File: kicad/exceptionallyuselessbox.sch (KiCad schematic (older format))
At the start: 10 parts, among them J1 Conn_01x02, J2 Conn_01x04, J3 Conn_01x02, J4 Conn_01x03, J5 Conn_01x03, U1 DSN-MINI-360

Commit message: Complete PCB.
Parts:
- C1, C2: value CP -> 100u; footprint (none) -> Capacitor_THT:CP_Radial_D8.0mm_P5.00mm
- J1, J3: footprint (none) -> Connector_JST:JST_XH_B02B-XH-A_1x02_P2.50mm_Vertical
- J2: footprint (none) -> Connector_JST:JST_XH_B04B-XH-A_1x04_P2.50mm_Vertical
- J4, J5: footprint (none) -> Connector_JST:JST_XH_B03B-XH-A_1x03_P2.50mm_Vertical
- R1: footprint (none) -> Resistor_THT:R_Axial_DIN0309_L9.0mm_D3.2mm_P12.70mm_Horizontal
- U1: footprint (none) -> Module:DSN-MINI-360
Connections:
- net +5V: no longer C2.1
- net +6V: now also C2.1
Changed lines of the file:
@@
 F 0 "J1" H 2568 2867 50  0000 C CNN
 F 1 "Conn_01x02" H 2568 2776 50  0000 C CNN
-F 2 "" H 2650 2650 50  0001 C CNN
+F 2 "Connector_JST:JST_XH_B02B-XH-A_1x02_P2.50mm_Vertical" H 2650 2650 50  0001 C CNN
 F 3 "~" H 2650 2650 50  0001 C CNN
 	1    2650 2650
@@
 F 0 "J2" H 2568 3817 50  0000 C CNN
 F 1 "Conn_01x04" H 2568 3726 50  0000 C CNN
-F 2 "" H 2650 3500 50  0001 C CNN
+F 2 "Connector_JST:JST_XH_B04B-XH-A_1x04_P2.50mm_Vertical" H 2650 3500 50  0001 C CNN
 F 3 "~" H 2650 3500 50  0001 C CNN
 	1    2650 3500
@@
 F 0 "R1" H 3420 2446 50  0000 L CNN
 F 1 "10k" H 3420 2355 50  0000 L CNN
-F 2 "" V 3280 2400 50  0001 C CNN
+F 2 "Resistor_THT:R_Axial_DIN0309_L9.0mm_D3.2mm_P12.70mm_Horizontal" V 3280 2400 50  0001 C CNN
 F 3 "~" H 3350 2400 50  0001 C CNN
 	1    3350 2400
@@
 F 0 "J4" H 5980 3042 50  0000 L CNN
 F 1 "Conn_01x03" H 5980 2951 50  0000 L CNN
-F 2 "" H 5900 3000 50  0001 C CNN
+F 2 "Connector_JST:JST_XH_B03B-XH-A_1x03_P2.50mm_Vertical" H 5900 3000 50  0001 C CNN
 F 3 "~" H 5900 3000 50  0001 C CNN
 	1    5900 3000
@@
 F 0 "J5" H 5980 3742 50  0000 L CNN
 F 1 "Conn_01x03" H 5980 3651 50  0000 L CNN
-F 2 "" H 5900 3700 50  0001 C CNN
+F 2 "Connector_JST:JST_XH_B03B-XH-A_1x03_P2.50mm_Vertical" H 5900 3700 50  0001 C CNN
 F 3 "~" H 5900 3700 50  0001 C CNN
 	1    5900 3700
@@
 P 7250 2400
 F 0 "C1" H 7368 2446 50  0000 L CNN
-F 1 "CP" H 7368 2355 50  0000 L CNN
-F 2 "" H 7288 2250 50  0001 C CNN
+F 1 "100u" H 7368 2355 50  0000 L CNN
+F 2 "Capacitor_THT:CP_Radial_D8.0mm_P5.00mm" H 7288 2250 50  0001 C CNN
 F 3 "~" H 7250 2400 50  0001 C CNN
 	1    7250 2400
@@
 P 7850 2400
 F 0 "C2" H 7968 2446 50  0000 L CNN
-F 1 "CP" H 7968 2355 50  0000 L CNN
-F 2 "" H 7888 2250 50  0001 C CNN
+F 1 "100u" H 7968 2355 50  0000 L CNN
+F 2 "Capacitor_THT:CP_Radial_D8.0mm_P5.00mm" H 7888 2250 50  0001 C CNN
 F 3 "~" H 7850 2400 50  0001 C CNN
 	1    7850 2400
@@
 	1    0    0    -1
 $EndComp
-$Comp
-L power:+5V #PWR016
-U 1 1 5D1A2DBA
-P 7850 2050
-F 0 "#PWR016" H 7850 1900 50  0001 C CNN
-F 1 "+5V" H 7865 2223 50  0000 C CNN
-F 2 "" H 7850 2050 50  0001 C CNN
-F 3 "" H 7850 2050 50  0001 C CNN
-	1    7850 2050
-	1    0    0    -1
-$EndComp
 Wire Wire Line
 	7850 2050 7850 2250
@@
 F 0 "J3" H 2568 5617 50  0000 C CNN
 F 1 "Conn_01x02" H 2568 5526 50  0000 C CNN
-F 2 "" H 2650 5400 50  0001 C CNN
+F 2 "Connector_JST:JST_XH_B02B-XH-A_1x02_P2.50mm_Vertical" H 2650 5400 50  0001 C CNN
 F 3 "~" H 2650 5400 50  0001 C CNN
 	1    2650 5400
@@
 F 0 "U1" H 3600 5765 50  0000 C CNN
 F 1 "DSN-MINI-360" H 3600 5674 50  0000 C CNN
-F 2 "" H 3600 5450 50  0001 C CNN
+F 2 "Module:DSN-MINI-360" H 3600 5450 50  0001 C CNN
 F 3 "regulator\\lm78xx.pdf" H 3600 5450 50  0001 C CNN
 	1    3600 5450
@@
 Wire Wire Line
 	5900 1900 5900 2000
+$Comp
+L power:+6V #PWR?
+U 1 1 5D20DD0B
+P 7850 2050
+F 0 "#PWR?" H 7850 1900 50  0001 C CNN
+F 1 "+6V" H 7865 2223 50  0000 C CNN
+F 2 "" H 7850 2050 50  0001 C CNN
+F 3 "" H 7850 2050 50  0001 C CNN
+	1    7850 2050
+	1    0    0    -1
+$EndComp
 $EndSCHEMATC

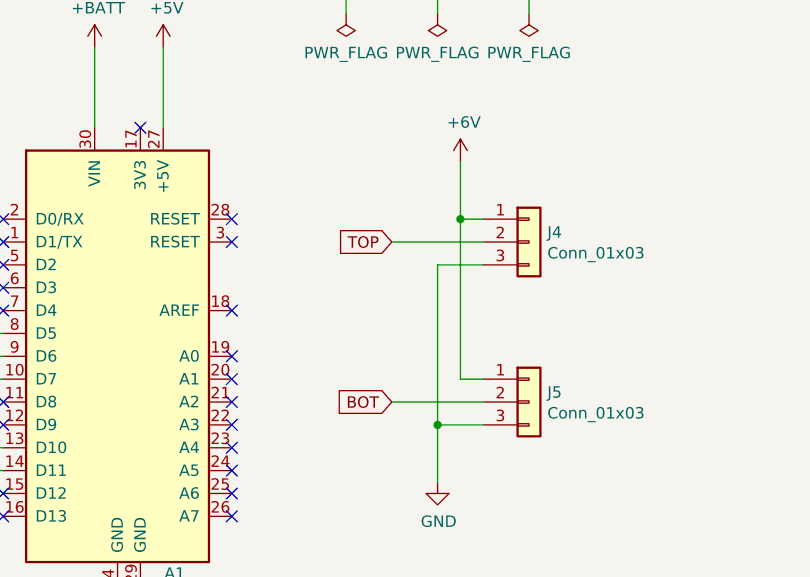
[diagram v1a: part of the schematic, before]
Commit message: Fix servo pinout.
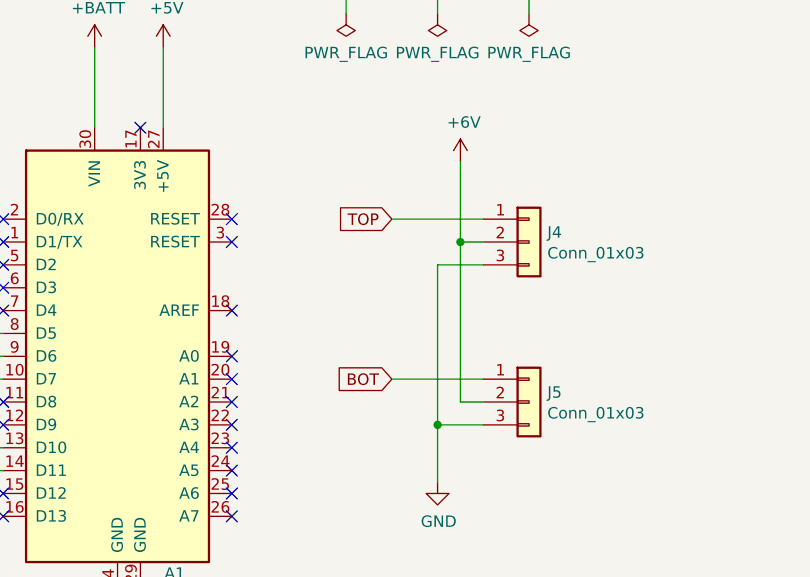
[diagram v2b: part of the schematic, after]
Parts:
- J4, J5: footprint Connector_JST:JST_XH_B03B-XH-A_1x03_P2.50mm_Vertical -> Connector_PinHeader_2.54mm:PinHeader_1x03_P2.54mm_Vertical
- R1: footprint Resistor_THT:R_Axial_DIN0309_L9.0mm_D3.2mm_P12.70mm_Horizontal -> Resistor_THT:R_Axial_DIN0207_L6.3mm_D2.5mm_P10.16mm_Horizontal
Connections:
- net +6V: now also J4.2 (Pin_2), J5.2 (Pin_2); no longer J4.1 (Pin_1), J5.1 (Pin_1)
- net BOT: now also J5.1 (Pin_1); no longer J5.2 (Pin_2)
- net TOP: now also J4.1 (Pin_1); no longer J4.2 (Pin_2)
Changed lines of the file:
@@
 F 0 "R1" H 3420 2446 50  0000 L CNN
 F 1 "10k" H 3420 2355 50  0000 L CNN
-F 2 "Resistor_THT:R_Axial_DIN0309_L9.0mm_D3.2mm_P12.70mm_Horizontal" V 3280 2400 50  0001 C CNN
+F 2 "Resistor_THT:R_Axial_DIN0207_L6.3mm_D2.5mm_P10.16mm_Horizontal" V 3280 2400 50  0001 C CNN
 F 3 "~" H 3350 2400 50  0001 C CNN
 	1    3350 2400
@@
 	1    0    0    -1
 $EndComp
-Wire Wire Line
-	5600 2650 5600 2900
-Wire Wire Line
-	5600 3600 5700 3600
-Wire Wire Line
-	5700 2900 5600 2900
-Connection ~ 5600 2900
-Wire Wire Line
-	5600 2900 5600 3600
 $Comp
 L Connector_Generic:Conn_01x03 J4
@@
 F 0 "J4" H 5980 3042 50  0000 L CNN
 F 1 "Conn_01x03" H 5980 2951 50  0000 L CNN
-F 2 "Connector_JST:JST_XH_B03B-XH-A_1x03_P2.50mm_Vertical" H 5900 3000 50  0001 C CNN
+F 2 "Connector_PinHeader_2.54mm:PinHeader_1x03_P2.54mm_Vertical" H 5900 3000 50  0001 C CNN
 F 3 "~" H 5900 3000 50  0001 C CNN
 	1    5900 3000
@@
 F 0 "J5" H 5980 3742 50  0000 L CNN
 F 1 "Conn_01x03" H 5980 3651 50  0000 L CNN
-F 2 "Connector_JST:JST_XH_B03B-XH-A_1x03_P2.50mm_Vertical" H 5900 3700 50  0001 C CNN
+F 2 "Connector_PinHeader_2.54mm:PinHeader_1x03_P2.54mm_Vertical" H 5900 3700 50  0001 C CNN
 F 3 "~" H 5900 3700 50  0001 C CNN
 	1    5900 3700
@@
 Wire Wire Line
 	5500 3800 5500 4050
-Text GLabel 5300 3000 0    50   Input ~ 0
+Text GLabel 5300 2900 0    50   Input ~ 0
 TOP
-Text GLabel 5300 3700 0    50   Input ~ 0
+Text GLabel 5300 3600 0    50   Input ~ 0
 BOT
-Wire Wire Line
-	5700 3700 5300 3700
-Wire Wire Line
-	5300 3000 5700 3000
 Text GLabel 3000 4200 0    50   Input ~ 0
 TOP
@@
 	5900 1900 5900 2000
 $Comp
-L power:+6V #PWR?
+L power:+6V #PWR0104
 U 1 1 5D20DD0B
 P 7850 2050
-F 0 "#PWR?" H 7850 1900 50  0001 C CNN
+F 0 "#PWR0104" H 7850 1900 50  0001 C CNN
 F 1 "+6V" H 7865 2223 50  0000 C CNN
 F 2 "" H 7850 2050 50  0001 C CNN
@@
 	1    0    0    -1
 $EndComp
+Wire Wire Line
+	5600 3700 5700 3700
+Wire Wire Line
+	5600 2650 5600 3000
+Wire Wire Line
+	5700 3000 5600 3000
+Connection ~ 5600 3000
+Wire Wire Line
+	5600 3000 5600 3700
+Wire Wire Line
+	5300 3600 5700 3600
+Wire Wire Line
+	5700 2900 5300 2900
 $EndSCHEMATC

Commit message: Update PCB.
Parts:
- removed U1: DSN-MINI-360, Module:DSN-MINI-360, symbol dsnmini360:DSN-MINI-360
- added L1: 10 mH, Inductor_THT:L_Radial_D9.5mm_P5.00mm_Fastron_07HVP, symbol Device:L
- added Q1: IRFZ44N, Package_TO_SOT_THT:TO-220-3_Vertical, symbol Device:Q_NMOS_GDS
- added R2: 1K, Resistor_THT:R_Axial_DIN0207_L6.3mm_D2.5mm_P5.08mm_Vertical, symbol Device:R
- added R3: 10K, Resistor_THT:R_Axial_DIN0207_L6.3mm_D2.5mm_P5.08mm_Vertical, symbol Device:R
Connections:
- net +5V: now also C1.1, J3.1 (Pin_1), L1.1
- net GND: now also Q1.3 (S), R3.1; no longer J4.3 (Pin_3), J5.3 (Pin_3)
- net SERVO_ON: now reaches A1.16 (D13)
- net SERVO_ON: now also R2.2, R3.2
- net +6V: no longer names the net of C2.1, J4.2 (Pin_2), J5.2 (Pin_2)
- net +6V: now also L1.2
- removed net +BATT: A1.30 (VIN), C1.1, J3.1 (Pin_1)
- new net: J4.3 (Pin_3), J5.3 (Pin_3), Q1.2 (D)
- new net: Q1.1 (G), R2.1
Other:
- moved on the sheet: C2
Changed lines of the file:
@@
 	3350 2100 3350 2250
-$Comp
-L power:GND #PWR012
-U 1 1 5D197190
-P 5500 4050
-F 0 "#PWR012" H 5500 3800 50  0001 C CNN
-F 1 "GND" H 5505 3877 50  0000 C CNN
-F 2 "" H 5500 4050 50  0001 C CNN
-F 3 "" H 5500 4050 50  0001 C CNN
-	1    5500 4050
-	1    0    0    -1
-$EndComp
 $Comp
 L Connector_Generic:Conn_01x03 J4
@@
 Wire Wire Line
 	5700 3800 5500 3800
-Connection ~ 5500 3800
-Wire Wire Line
-	5500 3800 5500 4050
 Text GLabel 5300 2900 0    50   Input ~ 0
 TOP
@@
 	4100 4700 4100 4500
 $Comp
-L power:+BATT #PWR07
-U 1 1 5D1A01AC
-P 4000 2150
-F 0 "#PWR07" H 4000 2000 50  0001 C CNN
-F 1 "+BATT" H 4015 2323 50  0000 C CNN
-F 2 "" H 4000 2150 50  0001 C CNN
-F 3 "" H 4000 2150 50  0001 C CNN
-	1    4000 2150
-	1    0    0    -1
-$EndComp
-$Comp
 L power:+5V #PWR010
 U 1 1 5D1A0909
@@
 Wire Wire Line
 	4300 2150 4300 2500
-Wire Wire Line
-	4000 2150 4000 2500
 $Comp
 L Device:CP C1
@@
 L Device:CP C2
 U 1 1 5D1A21BD
-P 7850 2400
-F 0 "C2" H 7968 2446 50  0000 L CNN
-F 1 "100u" H 7968 2355 50  0000 L CNN
-F 2 "Capacitor_THT:CP_Radial_D8.0mm_P5.00mm" H 7888 2250 50  0001 C CNN
-F 3 "~" H 7850 2400 50  0001 C CNN
-	1    7850 2400
+P 4100 5550
+F 0 "C2" H 4218 5596 50  0000 L CNN
+F 1 "100u" H 4218 5505 50  0000 L CNN
+F 2 "Capacitor_THT:CP_Radial_D8.0mm_P5.00mm" H 4138 5400 50  0001 C CNN
+F 3 "~" H 4100 5550 50  0001 C CNN
+	1    4100 5550
 	1    0    0    -1
 $EndComp
@@
 	1    0    0    -1
 $EndComp
-$Comp
-L power:+BATT #PWR014
-U 1 1 5D1A2A11
-P 7250 2050
-F 0 "#PWR014" H 7250 1900 50  0001 C CNN
-F 1 "+BATT" H 7265 2223 50  0000 C CNN
-F 2 "" H 7250 2050 50  0001 C CNN
-F 3 "" H 7250 2050 50  0001 C CNN
-	1    7250 2050
-	1    0    0    -1
-$EndComp
-Wire Wire Line
-	7850 2050 7850 2250
 Wire Wire Line
 	7250 2050 7250 2250
-Wire Wire Line
-	7250 2550 7250 2700
-Wire Wire Line
-	7850 2550 7850 2700
-Wire Wire Line
-	7850 2700 7250 2700
-Connection ~ 7250 2700
-Wire Wire Line
-	7250 2700 7250 2800
 $Comp
 L Connector_Generic:Conn_01x02 J3
@@
 Wire Wire Line
 	2850 5500 3050 5500
-Wire Wire Line
-	3050 5500 3050 5550
-Wire Wire Line
-	3050 5150 3050 5350
-$Comp
-L power:+BATT #PWR04
-U 1 1 5D18F4C8
-P 3050 5150
-F 0 "#PWR04" H 3050 5000 50  0001 C CNN
-F 1 "+BATT" H 3065 5323 50  0000 C CNN
-F 2 "" H 3050 5150 50  0001 C CNN
-F 3 "" H 3050 5150 50  0001 C CNN
-	1    3050 5150
-	1    0    0    -1
-$EndComp
-$Comp
-L power:+6V #PWR013
-U 1 1 5D1928AA
-P 5600 2650
-F 0 "#PWR013" H 5600 2500 50  0001 C CNN
-F 1 "+6V" H 5615 2823 50  0000 C CNN
-F 2 "" H 5600 2650 50  0001 C CNN
-F 3 "" H 5600 2650 50  0001 C CNN
-	1    5600 2650
-	1    0    0    -1
-$EndComp
-$Comp
-L dsnmini360:DSN-MINI-360 U1
-U 1 1 5D1930E1
-P 3600 5450
-F 0 "U1" H 3600 5765 50  0000 C CNN
-F 1 "DSN-MINI-360" H 3600 5674 50  0000 C CNN
-F 2 "Module:DSN-MINI-360" H 3600 5450 50  0001 C CNN
-F 3 "regulator\\lm78xx.pdf" H 3600 5450 50  0001 C CNN
-	1    3600 5450
-	1    0    0    -1
-$EndComp
-Wire Wire Line
-	3200 5550 3050 5550
-Connection ~ 3050 5550
-Wire Wire Line
-	3050 5550 3050 5700
-Wire Wire Line
-	3200 5350 3050 5350
-Connection ~ 3050 5350
-Wire Wire Line
-	3050 5350 3050 5400
-$Comp
-L power:GND #PWR09
-U 1 1 5D194B4C
-P 4200 5700
-F 0 "#PWR09" H 4200 5450 50  0001 C CNN
-F 1 "GND" H 4205 5527 50  0000 C CNN
-F 2 "" H 4200 5700 50  0001 C CNN
-F 3 "" H 4200 5700 50  0001 C CNN
-	1    4200 5700
-	1    0    0    -1
-$EndComp
-Wire Wire Line
-	4200 5700 4200 5550
-Wire Wire Line
-	4200 5550 4000 5550
-$Comp
-L power:+6V #PWR011
-U 1 1 5D195DF7
-P 4450 5200
-F 0 "#PWR011" H 4450 5050 50  0001 C CNN
-F 1 "+6V" H 4465 5373 50  0000 C CNN
-F 2 "" H 4450 5200 50  0001 C CNN
-F 3 "" H 4450 5200 50  0001 C CNN
-	1    4450 5200
-	1    0    0    -1
-$EndComp
-Wire Wire Line
-	4450 5200 4450 5350
-Wire Wire Line
-	4450 5350 4000 5350
 NoConn ~ 4600 2900
 NoConn ~ 4600 3000
@@
 NoConn ~ 4600 4100
 NoConn ~ 4600 4200
-NoConn ~ 3600 4200
 NoConn ~ 3600 4100
 NoConn ~ 3600 3800
@@
 	-1   0    0    1
 $EndComp
-$Comp
-L power:+BATT #PWR0101
-U 1 1 5D1AA6E2
-P 5100 1900
-F 0 "#PWR0101" H 5100 1750 50  0001 C CNN
-F 1 "+BATT" H 5115 2073 50  0000 C CNN
-F 2 "" H 5100 1900 50  0001 C CNN
-F 3 "" H 5100 1900 50  0001 C CNN
-	1    5100 1900
-	1    0    0    -1
-$EndComp
 Wire Wire Line
 	5100 1900 5100 2000
@@
 Wire Wire Line
 	5500 1900 5500 2000
-$Comp
-L power:PWR_FLAG #FLG0103
-U 1 1 5D1AEBC8
-P 5900 2000
-F 0 "#FLG0103" H 5900 2075 50  0001 C CNN
-F 1 "PWR_FLAG" H 5900 2173 50  0000 C CNN
-F 2 "" H 5900 2000 50  0001 C CNN
-F 3 "~" H 5900 2000 50  0001 C CNN
-	1    5900 2000
-	-1   0    0    1
-$EndComp
-$Comp
-L power:+6V #PWR0103
-U 1 1 5D1AF2A5
-P 5900 1900
-F 0 "#PWR0103" H 5900 1750 50  0001 C CNN
-F 1 "+6V" H 5915 2073 50  0000 C CNN
-F 2 "" H 5900 1900 50  0001 C CNN
-F 3 "" H 5900 1900 50  0001 C CNN
-	1    5900 1900
-	1    0    0    -1
-$EndComp
-Wire Wire Line
-	5900 1900 5900 2000
-$Comp
-L power:+6V #PWR0104
-U 1 1 5D20DD0B
-P 7850 2050
-F 0 "#PWR0104" H 7850 1900 50  0001 C CNN
-F 1 "+6V" H 7865 2223 50  0000 C CNN
-F 2 "" H 7850 2050 50  0001 C CNN
-F 3 "" H 7850 2050 50  0001 C CNN
-	1    7850 2050
-	1    0    0    -1
-$EndComp
 Wire Wire Line
 	5600 3700 5700 3700
 Wire Wire Line
-	5600 2650 5600 3000
-Wire Wire Line
 	5700 3000 5600 3000
-Connection ~ 5600 3000
 Wire Wire Line
 	5600 3000 5600 3700
@@
 Wire Wire Line
 	5700 2900 5300 2900
+$Comp
+L Device:Q_NMOS_GDS Q1
+U 1 1 5D426E91
+P 3700 6150
+F 0 "Q1" H 3906 6196 50  0000 L CNN
+F 1 "IRFZ44N" H 3906 6105 50  0000 L CNN
+F 2 "Package_TO_SOT_THT:TO-220-3_Vertical" H 3900 6250 50  0001 C CNN
+F 3 "~" H 3700 6150 50  0001 C CNN
+	1    3700 6150
+	1    0    0    -1
+$EndComp
+Text GLabel 2850 6150 0    50   Input ~ 0
+SERVO_ON
+Wire Wire Line
+	3800 6550 3800 6350
+Text GLabel 3000 4700 0    50   Input ~ 0
+SERVO_ON
+Wire Wire Line
+	3000 4700 3500 4700
+Wire Wire Line
+	3500 4700 3500 4200
+Wire Wire Line
+	3500 4200 3600 4200
+Wire Wire Line
+	3050 5150 3050 5400
+Wire Wire Line
+	3050 5500 3050 5700
+$Comp
+L power:+5V #PWR0101
+U 1 1 5D433C1B
+P 3050 5150
+F 0 "#PWR0101" H 3050 5000 50  0001 C CNN
+F 1 "+5V" H 3065 5323 50  0000 C CNN
+F 2 "" H 3050 5150 50  0001 C CNN
+F 3 "" H 3050 5150 50  0001 C CNN
+	1    3050 5150
+	1    0    0    -1
+$EndComp
+$Comp
+L Device:L L1
+U 1 1 5D43549D
+P 3350 5400
+F 0 "L1" V 3540 5400 50  0000 C CNN
+F 1 "10 mH" V 3449 5400 50  0000 C CNN
+F 2 "Inductor_THT:L_Radial_D9.5mm_P5.00mm_Fastron_07HVP" H 3350 5400 50  0001 C CNN
+F 3 "~" H 3350 5400 50  0001 C CNN
+	1    3350 5400
+	0    -1   -1   0
+$EndComp
+Wire Wire Line
+	3200 5400 3050 5400
+Connection ~ 3050 5400
+Wire Wire Line
+	7250 2550 7250 2800
+$Comp
+L power:+5V #PWR0104
+U 1 1 5D44F2C4
+P 7250 2050
+F 0 "#PWR0104" H 7250 1900 50  0001 C CNN
+F 1 "+5V" H 7265 2223 50  0000 C CNN
+F 2 "" H 7250 2050 50  0001 C CNN
+F 3 "" H 7250 2050 50  0001 C CNN
+	1    7250 2050
+	1    0    0    -1
+$EndComp
+$Comp
+L power:+5V #PWR0105
+U 1 1 5D44FFFE
+P 5100 1900
+F 0 "#PWR0105" H 5100 1750 50  0001 C CNN
+F 1 "+5V" H 5115 2073 50  0000 C CNN
+F 2 "" H 5100 1900 50  0001 C CNN
+F 3 "" H 5100 1900 50  0001 C CNN
+	1    5100 1900
+	1    0    0    -1
+$EndComp
+NoConn ~ 4000 2500
+$Comp
+L Device:R R2
+U 1 1 5D4624B6
+P 3250 6150
+F 0 "R2" V 3043 6150 50  0000 C CNN
+F 1 "1K" V 3134 6150 50  0000 C CNN
+F 2 "Resistor_THT:R_Axial_DIN0207_L6.3mm_D2.5mm_P5.08mm_Vertical" V 3180 6150 50  0001 C CNN
+F 3 "~" H 3250 6150 50  0001 C CNN
+	1    3250 6150
+	0    1    1    0
+$EndComp
+$Comp
+L Device:R R3
+U 1 1 5D462815
+P 3250 6550
+F 0 "R3" V 3043 6550 50  0000 C CNN
+F 1 "10K" V 3134 6550 50  0000 C CNN
+F 2 "Resistor_THT:R_Axial_DIN0207_L6.3mm_D2.5mm_P5.08mm_Vertical" V 3180 6550 50  0001 C CNN
+F 3 "~" H 3250 6550 50  0001 C CNN
+	1    3250 6550
+	0    1    1    0
+$EndComp
+Wire Wire Line
+	3500 6150 3400 6150
+Wire Wire Line
+	2850 6150 3000 6150
+Wire Wire Line
+	3000 6150 3000 6550
+Wire Wire Line
+	3000 6550 3100 6550
+Connection ~ 3000 6150
+Wire Wire Line
+	3000 6150 3100 6150
+$Comp
+L power:GND #PWR?
+U 1 1 5D4704C0
+P 3550 6650
+F 0 "#PWR?" H 3550 6400 50  0001 C CNN
+F 1 "GND" H 3555 6477 50  0000 C CNN
+F 2 "" H 3550 6650 50  0001 C CNN
+F 3 "" H 3550 6650 50  0001 C CNN
+	1    3550 6650
+	1    0    0    -1
+$EndComp
+Wire Wire Line
+	3550 6650 3550 6550
+Wire Wire Line
+	3550 6550 3400 6550
+Wire Wire Line
+	3500 5400 4100 5400
+Wire Wire Line
+	4100 5400 5600 5400
+Wire Wire Line
+	5600 5400 5600 3700
+Connection ~ 4100 5400
+Connection ~ 5600 3700
+Wire Wire Line
+	4100 6550 3800 6550
+Wire Wire Line
+	4100 5700 4100 6550
+Connection ~ 3550 6550
+Connection ~ 3800 6550
+Wire Wire Line
+	3800 6550 3550 6550
+Wire Wire Line
+	3800 5950 3800 5800
+Wire Wire Line
+	3800 5800 5500 5800
+Wire Wire Line
+	5500 5800 5500 3800
+Connection ~ 5500 3800
 $EndSCHEMATC

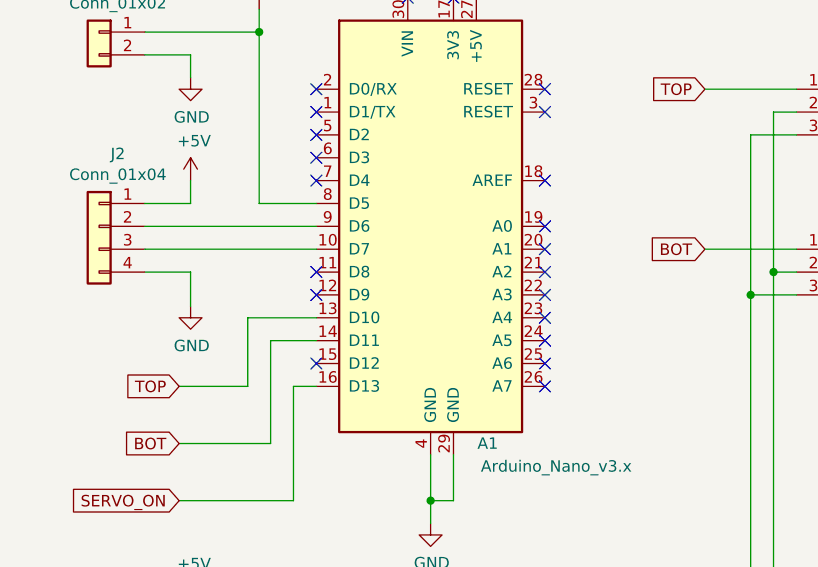
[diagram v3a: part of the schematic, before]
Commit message: Use I2C sensor.
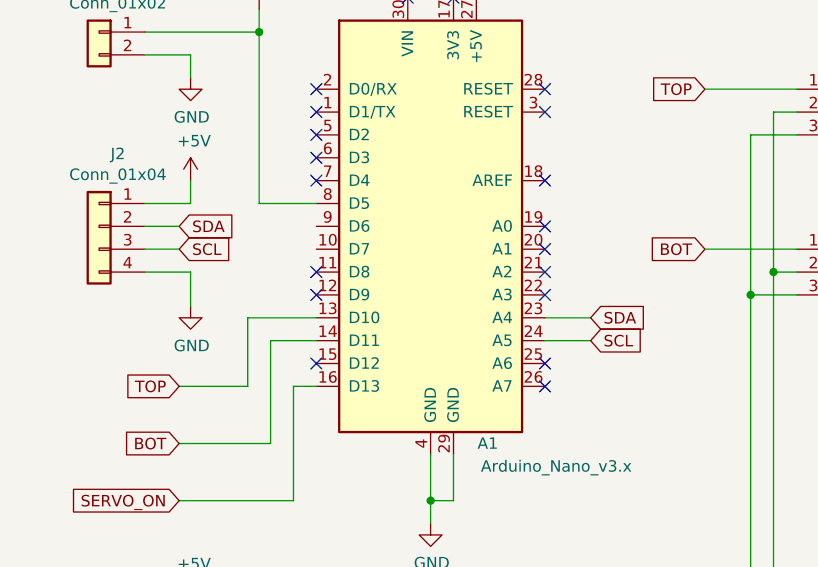
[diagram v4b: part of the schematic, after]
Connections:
- net at A1.10 (D7): no longer J2.3 (Pin_3)
- net SDA: now reaches A1.23 (A4)
- net SDA: now also J2.2 (Pin_2)
- net SCL: now reaches A1.24 (A5)
- net SCL: now also J2.3 (Pin_3)
- net at A1.9 (D6): no longer J2.2 (Pin_2)
- no-connect marks 21 -> 19
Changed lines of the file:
@@
 	-1   0    0    -1
 $EndComp
-Wire Wire Line
-	3600 3500 2850 3500
-Wire Wire Line
-	2850 3600 3600 3600
 $Comp
 L power:+5V #PWR02
@@
 NoConn ~ 4600 3700
 NoConn ~ 4600 3800
-NoConn ~ 4600 3900
-NoConn ~ 4600 4000
 NoConn ~ 4600 4100
 NoConn ~ 4600 4200
@@
 	5500 5800 5500 3800
 Connection ~ 5500 3800
+Text GLabel 3000 3500 2    50   Input ~ 0
+SDA
+Text GLabel 3000 3600 2    50   Input ~ 0
+SCL
+Wire Wire Line
+	3000 3600 2850 3600
+Wire Wire Line
+	2850 3500 3000 3500
+Text GLabel 4800 3900 2    50   Input ~ 0
+SDA
+Wire Wire Line
+	4800 3900 4600 3900
+Text GLabel 4800 4000 2    50   Input ~ 0
+SCL
+Wire Wire Line
+	4800 4000 4600 4000
 $EndSCHEMATC
